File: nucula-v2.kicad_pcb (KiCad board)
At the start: 4 copper layers, 60 x 110 mm, 131 parts, among them J1 USB4105-GF-A-120, J2 JST-PH / 1S Li-ion, J3 KEYBOARD / USER FIT, J4 MAIN LINK / OPTIONAL, J5 MODULE LINK / OPTIONAL, Q1 IRLML6402, Q2 BSS138, Q3 IRLML6402, Q4 BSS138, Q5 BSS138, SW1 RESET, SW2 BOOT, U1 TP4054-42-SOT25R, U10 TS3USB30EDGSR, U2 SY8089AAAC, U3 ESP32-C3-WROOM-02-N4, U4 TPD2E2U06QDCKRQ1, U5 TLV803EA30DBZR, U6 PN7160A1HN/C100E, U7 AP3012KTR-E1, U8 PCF8574T, U9 MCP1700T-3002E/TT, Y1 27.12MHz / CL 10pF

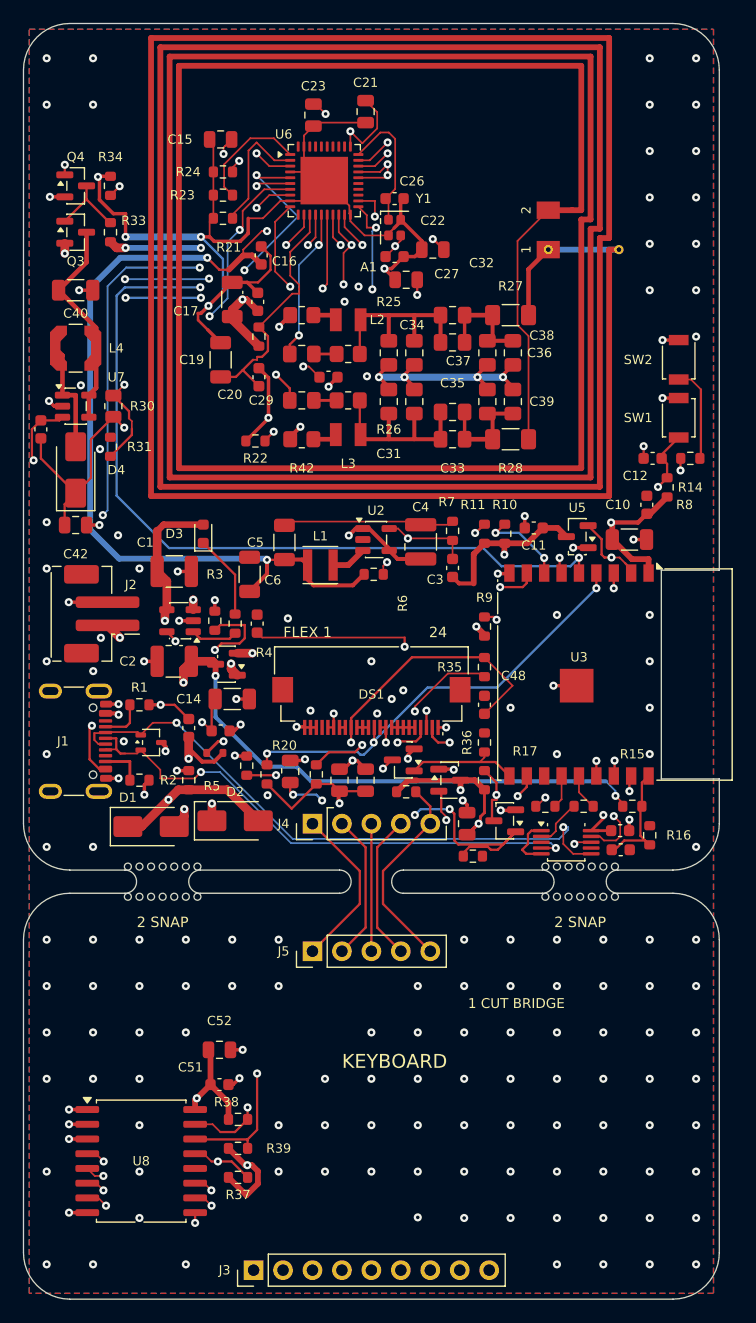
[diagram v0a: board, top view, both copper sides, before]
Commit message: Switch to ESP32-C3-MINI-1 with a flush antenna cutout
Replace WROOM-02 with MINI-1-H4X while preserving GPIO assignments and
4 MB flash. Resize the antenna notch and align the antenna tip with the
PCB edge; update the schematic, routing, footprint, model and BOM.

Include the current JST-SH battery connector and direct battery solder
pads, plus manufacturing archives and the new MINI prototype package.
Record ESP-IDF 5.4+ compatibility and the remaining physical validation.

Validation: zero ERC/DRC errors or unconnected nets; 17 MINI checks,
16 fabrication checks, six routing checks and 30 export checks pass.
The 261 scoped simulation cases completed without solver errors.
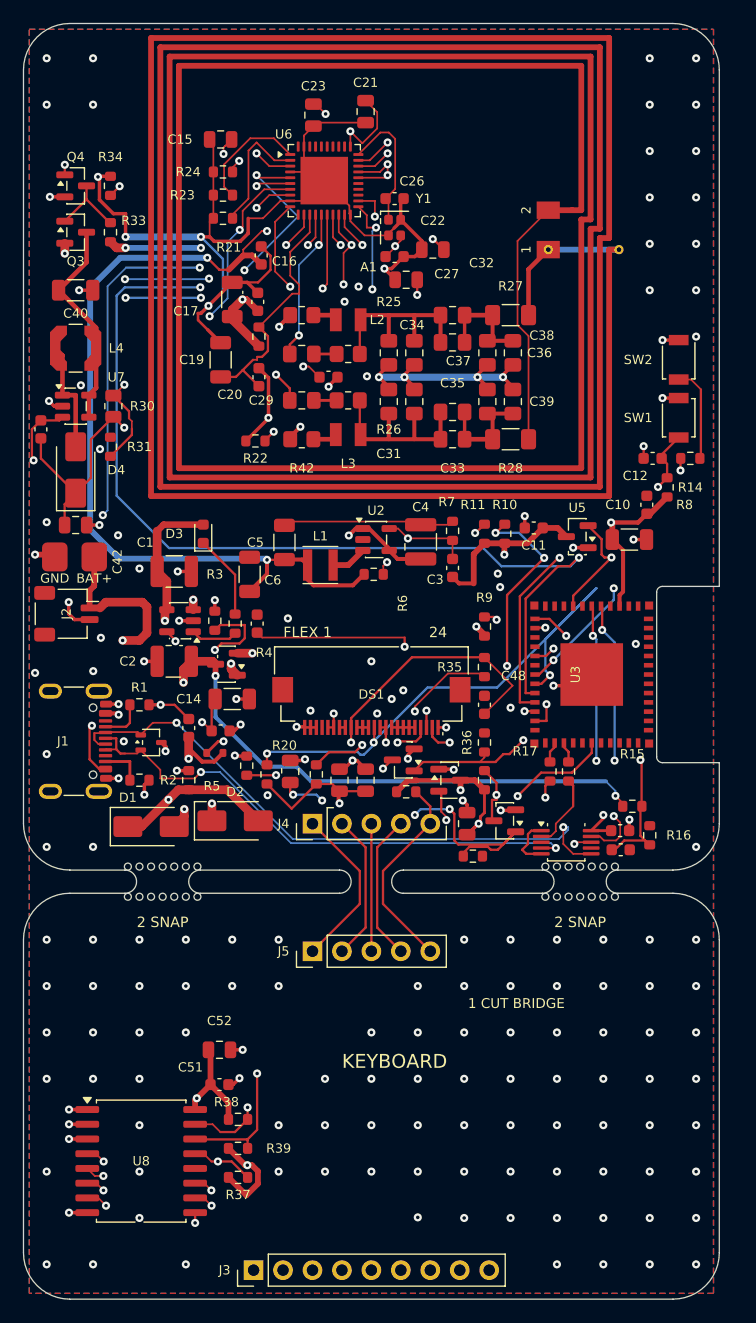
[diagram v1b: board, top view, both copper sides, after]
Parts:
- added J6: Battery wire pads, Nucula_Project:Battery_Lead_SolderPads_2x2.2x2.5mm_P3.4mm, F.Cu at (54.4, 96.0)
- J2: value JST-PH / 1S Li-ion -> JST-SH / 1S Li-ion; footprint Nucula_Project:JST_PH_B2B-PH-SM4-TB_1x02-1MP_P2.00mm_Vertical -> Nucula_Project:JST_SH_SM02B-SRSS-TB_1x02-1MP_P1.00mm_Horizontal
- U3: value ESP32-C3-WROOM-02-N4 -> ESP32-C3-MINI-1-H4X; footprint Nucula_Project:ESP32-C3-WROOM-02-N4_NoEPADSolder -> Nucula_Project:ESP32-C3-MINI-1-H4X_NoEPADSolder
- moved U3 3.80 mm to (101.7, 106.1)
- moved R13 3.27 mm to (97.0, 114.5), turned to 90 degrees
- moved J2 3.05 mm to (53.7, 100.9), turned to -90 degrees
- moved R12 3.03 mm to (95.4, 114.5), turned to 90 degrees
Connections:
- U3 pad 1: /+3V3 -> GND
- U3 pad 10: /OLED_RESET -> unconnected-(U3-NC-Pad10)
- U3 pad 11: /KEY_INT_N -> GND
- U3 pad 12: unconnected-(U3-IO21/TXD-Pad12) -> /Power + ESP32-C3/VBAT_ADC
- U3 pad 13: Net-(U3-IO18) -> /Power + ESP32-C3/USB_PRESENT_N
- U3 pad 14: Net-(U3-IO19) -> GND
- U3 pad 15: /OLED_PWR_EN -> unconnected-(U3-NC-Pad15)
- U3 pad 16: /Power + ESP32-C3/STRAP_GPIO2 -> /OLED_RESET
- U3 pad 17: /Power + ESP32-C3/USB_PRESENT_N -> unconnected-(U3-NC-Pad17)
- U3 pad 18: /Power + ESP32-C3/VBAT_ADC -> /I2C_SDA
- U3 pad 19: GND -> /I2C_SCL
- U3 pad 2: /Power + ESP32-C3/ESP_EN -> GND
- U3 pad 3: /I2C_SDA -> /+3V3
- U3 pad 4: /I2C_SCL -> unconnected-(U3-NC-Pad4)
- U3 pad 5: /NFC_IRQ -> /Power + ESP32-C3/STRAP_GPIO2
- U3 pad 6: /NFC_VEN -> /OLED_PWR_EN
- U3 pad 7: /Power + ESP32-C3/STRAP_GPIO8 -> unconnected-(U3-NC-Pad7)
- U3 pad 8: /Power + ESP32-C3/BOOT_N -> /Power + ESP32-C3/ESP_EN
- U3 pad 9: GND -> unconnected-(U3-NC-Pad9)
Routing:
- net /Power + ESP32-C3/VBAT_ADC: track 10.4 -> 28.2 mm, vias 0 -> 2
- net /Power + ESP32-C3/USB_PRESENT_N: track 26.2 -> 42.9 mm
- net /Power + ESP32-C3/STRAP_GPIO8: track 7.51 -> 22.3 mm, vias 2 -> 4
- net /NFC_VEN: track 105.6 -> 119.4 mm
- net /NFC_IRQ: track 83.8 -> 97.5 mm
- net /OLED_RESET: track 10.1 -> 23.0 mm, vias 0 -> 2
- net /Power + ESP32-C3/VBAT: track 64.5 -> 77.2 mm
- net /Power + ESP32-C3/STRAP_GPIO2: track 18.9 -> 31.3 mm, vias 2 -> 3
- net /OLED_PWR_EN: track 100.0 -> 112.2 mm, vias 4 -> 5
- net /Power + ESP32-C3/BOOT_N: track 31.2 -> 42.1 mm, vias 3 -> 4
- net /I2C_SCL: track 166.0 -> 175.8 mm
- net /I2C_SDA: track 164.0 -> 173.2 mm, vias 8 -> 9
- net /KEY_INT_N: track 59.7 -> 66.5 mm
- net /Power + ESP32-C3/ESP_EN: track 19.5 -> 22.6 mm
- net /Power + ESP32-C3/USB_PHY_D+: track 4.26 -> 6.55 mm
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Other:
- outline, holes or cut-outs redrawn

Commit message: Add six M2 mounting holes and validate the hardware revision
Place 2.2 mm NPTH holes at all four main-board corners and the two
lower keyboard corners. Reserve 5.5 mm copper and component clearances
for hardware up to 5 mm across, and move R16 with local ADC rerouting.
Preserve the MINI antenna fit, board outline and breakaway connections.

Add mechanical clearance checks, a dimensioned mounting plan and the
mounting-2026-10-08 manufacturing package with verified drill data.

Validation: zero ERC/DRC errors, unconnected nets or parity findings;
10 mounting checks, 32 export checks and 13 regression tests pass.
All 261 scoped simulations complete without solver errors. Existing
cosmetic warnings and USB layout advisories are unchanged.
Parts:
- added H1: M2 2.2mm NPTH, Nucula_Project:MountingHole_2.2mm_M2_5.5mm_Keepout, F.Cu at (53.5, 53.5)
- added H2: M2 2.2mm NPTH, Nucula_Project:MountingHole_2.2mm_M2_5.5mm_Keepout, F.Cu at (106.5, 53.5)
- added H3: M2 2.2mm NPTH, Nucula_Project:MountingHole_2.2mm_M2_5.5mm_Keepout, F.Cu at (53.5, 120.0)
- added H4: M2 2.2mm NPTH, Nucula_Project:MountingHole_2.2mm_M2_5.5mm_Keepout, F.Cu at (106.5, 120.0)
- added H5: M2 2.2mm NPTH, Nucula_Project:MountingHole_2.2mm_M2_5.5mm_Keepout, F.Cu at (53.5, 156.5)
- added H6: M2 2.2mm NPTH, Nucula_Project:MountingHole_2.2mm_M2_5.5mm_Keepout, F.Cu at (106.5, 156.5)
- moved R16 4.37 mm to (105.0, 115.8)
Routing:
- net GND: vias 174 -> 163

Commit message: Label PCB buttons BOOT and RESET on the silkscreen
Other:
- board text added: "BOOT"
- board text added: "RESET"
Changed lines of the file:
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@@
 		(tags "Tactile Switch")
 		(property "Reference" "SW1"
-			(at 0 -3.5 0)
-			(layer "F.SilkS")
+			(at 0 0 0)
+			(layer "F.Fab")
 			(effects
 				(font
@@
 			(layer "F.Fab")
 		)
-		(fp_text user "${REFERENCE}"
-			(at 0 -2.5 90)
-			(layer "F.Fab")
-			(effects
-				(font
-					(size 1 1)
-					(thickness 0.15)
-				)
-			)
-		)
 		(pad "1" smd rect
 			(at -1.7 0 90)
@@
 		(tags "Tactile Switch")
 		(property "Reference" "SW2"
-			(at 0 -3.5 0)
-			(layer "F.SilkS")
+			(at 0 0 0)
+			(layer "F.Fab")
 			(effects
 				(font
@@
 			(layer "F.Fab")
 		)
-		(fp_text user "${REFERENCE}"
-			(at 0 -2.5 90)
-			(layer "F.Fab")
-			(effects
-				(font
-					(size 1 1)
-					(thickness 0.15)
-				)
-			)
-		)
 		(pad "1" smd rect
 			(at -1.7 0 90)
@@
 		(layer "Edge.Cuts")
 	)
+	(gr_text "RESET"
+		(at 103 84 0)
+		(layer "F.SilkS")
+		(effects
+			(font
+				(size 0.8 0.8)
+				(thickness 0.12)
+			)
+		)
+	)
+	(gr_text "BOOT"
+		(at 103 79 0)
+		(layer "F.SilkS")
+		(effects
+			(font
+				(size 0.8 0.8)
+				(thickness 0.12)
+			)
+		)
+	)
 	(gr_text "1 CUT BRIDGE"

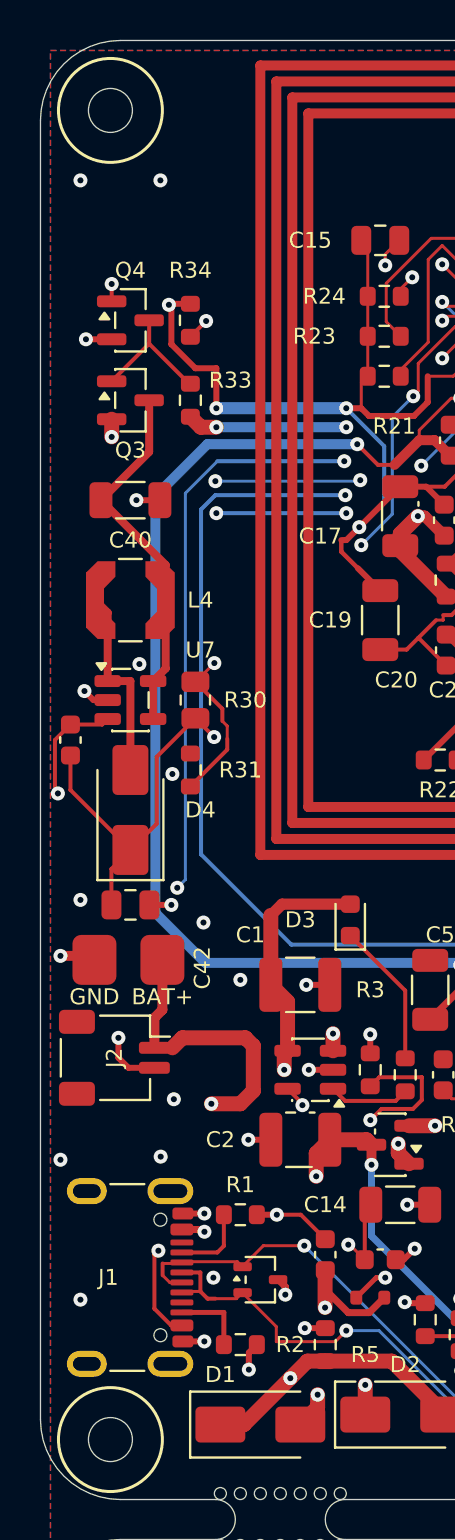
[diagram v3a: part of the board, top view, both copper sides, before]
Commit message: move jst connector, add notch for batt cable
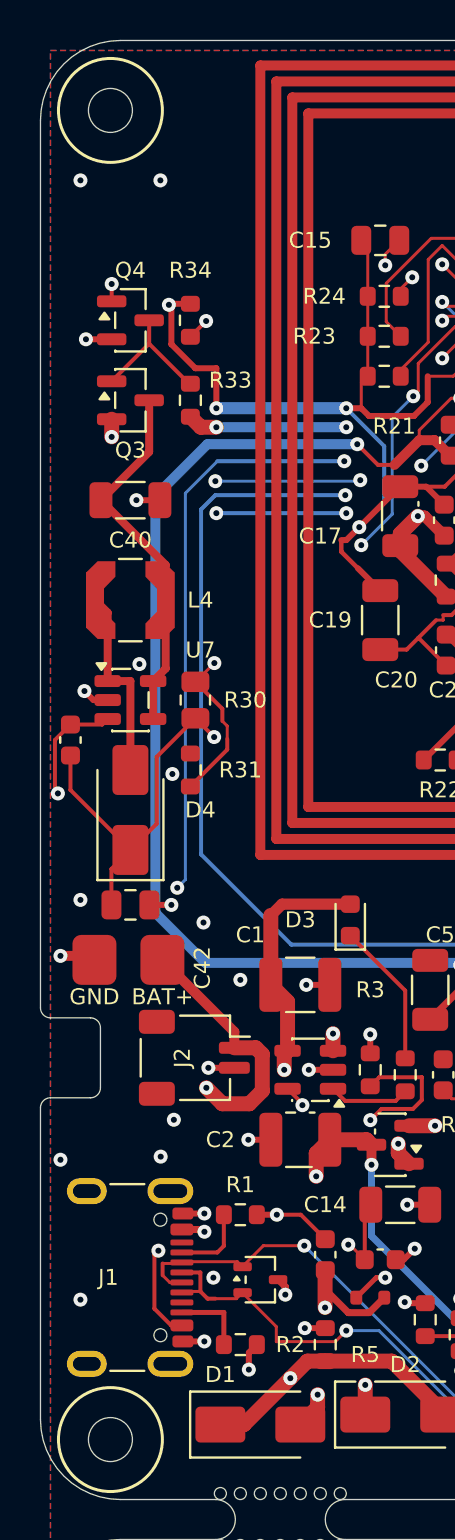
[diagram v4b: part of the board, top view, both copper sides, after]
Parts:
- moved J2 4.00 mm to (57.7, 100.9)
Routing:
- net GND: track 250.2 -> 248.5 mm
- net /Power + ESP32-C3/VBAT: track 77.2 -> 75.9 mm
- net /I2C_SCL: track 175.8 -> 176.4 mm
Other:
- outline, holes or cut-outs redrawn
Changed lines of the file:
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@@
 		(locked yes)
 		(layer "F.Cu")
-		(at 53.7 100.9 -90)
+		(at 57.7 100.9 -90)
 		(descr "JST SH series connector, SM02B-SRSS-TB (http://www.jst-mfg.com/product/pdf/eng/eSH.pdf)")
 		(tags "connector JST SH horizontal")
 		(property "Reference" "J2"
-			(at 0 0 90)
+			(at 0 0.6 90)
 			(layer "F.SilkS")
 			(effects
@@
 		(layer "Dwgs.User")
 	)
+	(gr_line
+		(start 50 54)
+		(end 50 98.4)
+		(stroke
+			(width 0.05)
+			(type default)
+		)
+		(layer "Edge.Cuts")
+	)
 	(gr_arc
 		(start 50 54)
@@
 	)
 	(gr_line
-		(start 50 119)
-		(end 50 54)
+		(start 50 103.4)
+		(end 50 119)
 		(stroke
 			(width 0.05)
-			(type solid)
+			(type default)
+		)
+		(layer "Edge.Cuts")
+	)
+	(gr_arc
+		(start 50 103.4)
+		(mid 50.146447 103.046447)
+		(end 50.5 102.9)
+		(stroke
+			(width 0.05)
+			(type default)
 		)
 		(layer "Edge.Cuts")
@@
 		(layer "Edge.Cuts")
 	)
+	(gr_arc
+		(start 50.5 98.9)
+		(mid 50.146447 98.753553)
+		(end 50 98.4)
+		(stroke
+			(width 0.05)
+			(type default)
+		)
+		(layer "Edge.Cuts")
+	)
+	(gr_line
+		(start 50.5 98.9)
+		(end 52.5 98.9)
+		(stroke
+			(width 0.05)
+			(type default)
+		)
+		(layer "Edge.Cuts")
+	)
+	(gr_arc
+		(start 52.5 98.9)
+		(mid 52.853553 99.046447)
+		(end 53 99.4)
+		(stroke
+			(width 0.05)
+			(type default)
+		)
+		(layer "Edge.Cuts")
+	)
+	(gr_line
+		(start 52.5 102.9)
+		(end 50.5 102.9)
+		(stroke
+			(width 0.05)
+			(type default)
+		)
+		(layer "Edge.Cuts")
+	)
+	(gr_line
+		(start 53 99.4)
+		(end 53 102.4)
+		(stroke
+			(width 0.05)
+			(type default)
+		)
+		(layer "Edge.Cuts")
+	)
+	(gr_arc
+		(start 53 102.4)
+		(mid 52.853553 102.753553)
+		(end 52.5 102.9)
+		(stroke
+			(width 0.05)
+			(type default)
+		)
+		(layer "Edge.Cuts")
+	)
 	(gr_line
 		(start 54 50)
@@
 		(layer "Edge.Cuts")
 	)
-	(gr_text "RESET"
-		(at 103 84 0)
+	(gr_text "BOOT"
+		(at 103 79 0)
 		(layer "F.SilkS")
 		(effects
@@
 		)
 	)
-	(gr_text "BOOT"
-		(at 103 79 0)
+	(gr_text "RESET"
+		(at 103 84 0)
 		(layer "F.SilkS")
 		(effects
@@
 	)
 	(segment
-		(start 54.4 101.4)
-		(end 55.7 101.4)
-		(width 0.3)
-		(layer "F.Cu")
-		(net "GND")
-	)
-	(segment
 		(start 78.1 66.4)
 		(end 78.1875 66.4875)
@@
 	)
 	(segment
+		(start 59.7 101.4)
+		(end 58.4 101.4)
+		(width 0.3)
+		(layer "F.Cu")
+		(net "GND")
+	)
+	(segment
 		(start 65.95 74.35)
 		(end 67.975 72.325)
@@
 	)
 	(segment
-		(start 53.9 100.9)
-		(end 54.4 101.4)
-		(width 0.3)
-		(layer "F.Cu")
-		(net "GND")
-	)
-	(segment
 		(start 60.425 115.65)
 		(end 60.825 115.25)
@@
 	)
 	(segment
-		(start 53.9 99.9)
-		(end 53.9 100.9)
-		(width 0.3)
-		(layer "F.Cu")
-		(net "GND")
-	)
-	(segment
 		(start 87.05 114.3)
 		(end 87.1 114.35)
@@
 	)
 	(via
-		(at 53.9 99.9)
+		(at 58.4 101.4)
 		(size 0.7)
 		(drill 0.3)
@@
 	)
 	(via
-		(at 56.6734 102.972)
+		(at 56.6734 104)
 		(size 0.7)
 		(drill 0.3)
@@
 	)
 	(segment
+		(start 60.7194 108.046)
+		(end 61.7474 108.046)
+		(width 0.2)
+		(layer "In1.Cu")
+		(net "/I2C_SCL")
+	)
+	(segment
 		(start 62.1779 108.046)
 		(end 69.04195 114.91005)
@@
 	)
 	(segment
-		(start 56.6734 102.972)
-		(end 61.7474 108.046)
+		(start 56.6734 104)
+		(end 60.7194 108.046)
 		(width 0.2)
 		(layer "In1.Cu")
@@
 	)
 	(segment
-		(start 57.5 102.1454)
+		(start 57.5 103.1734)
 		(end 57.5 73.3)
 		(width 0.15)
@@
 	)
 	(segment
-		(start 80.2 111.999)
-		(end 82.54 114.339)
-		(width 0.2)
+		(start 56.6734 104)
+		(end 57.5 103.1734)
+		(width 0.15)
 		(layer "In2.Cu")
 		(net "/I2C_SCL")
 	)
 	(segment
-		(start 56.6734 102.972)
-		(end 57.5 102.1454)
-		(width 0.15)
+		(start 80.2 111.999)
+		(end 82.54 114.339)
+		(width 0.2)
 		(layer "In2.Cu")
 		(net "/I2C_SCL")
@@
 	)
 	(segment
-		(start 60.65 100.3)
-		(end 60.65 102.55)
-		(width 0.75)
+		(start 56.1 96)
+		(end 59.7 99.6)
+		(width 0.5)
 		(layer "F.Cu")
 		(net "/Power + ESP32-C3/VBAT")
 	)
 	(segment
-		(start 60.25 99.9)
-		(end 60.65 100.3)
+		(start 61.1 100.725)
+		(end 61.1 102.55)
 		(width 0.75)
 		(layer "F.Cu")
@@
 	)
 	(segment
-		(start 55.7 98.9)
-		(end 55.7 100.4)
-		(width 0.5)
-		(layer "F.Cu")
-		(net "/Power + ESP32-C3/VBAT")
-	)
-	(segment
-		(start 101.675 117.225)
-		(end 101.675 117.5)
-		(width 0.15)
+		(start 60.45 103.2)
+		(end 59.1 103.2)
+		(width 0.75)
 		(layer "F.Cu")
 		(net "/Power + ESP32-C3/VBAT")
 	)
 	(segment
-		(start 60 103.2)
-		(end 58.55 103.2)
+		(start 61.1 102.55)
+		(end 60.45 103.2)
 		(width 0.75)
 		(layer "F.Cu")
@@
 	)
 	(segment
-		(start 55.7 100.4)
-		(end 56.6 100.4)
-		(width 0.4)
+		(start 101.675 117.225)
+		(end 101.675 117.5)
+		(width 0.15)
 		(layer "F.Cu")
 		(net "/Power + ESP32-C3/VBAT")
@@
 	)
 	(segment
-		(start 57.1 99.9)
-		(end 60.25 99.9)
+		(start 59.7 99.6)
+		(end 59.7 100.4)
+		(width 0.5)
+		(layer "F.Cu")
+		(net "/Power + ESP32-C3/VBAT")
+	)
+	(segment
+		(start 60.775 100.4)
+		(end 61.1 100.725)
 		(width 0.75)
 		(layer "F.Cu")
@@
 	)
 	(segment
-		(start 60.65 102.55)
-		(end 60 103.2)
+		(start 59.7 100.4)
+		(end 60.775 100.4)
 		(width 0.75)
 		(layer "F.Cu")
@@
 	)
 	(segment
-		(start 56.6 100.4)
-		(end 57.1 99.9)
-		(width 0.75)
-		(layer "F.Cu")
-		(net "/Power + ESP32-C3/VBAT")
-	)
-	(segment
-		(start 56.1 96)
-		(end 56.1 98.5)
-		(width 0.5)
-		(layer "F.Cu")
-		(net "/Power + ESP32-C3/VBAT")
-	)
-	(segment
 		(start 63.7957 106.83)
 		(end 63.7957 105.6793)
@@
 	)
 	(segment
-		(start 56.1 98.5)
-		(end 55.7 98.9)
-		(width 0.5)
+		(start 59.1 103.2)
+		(end 58.3 102.4)
+		(width 0.75)
 		(layer "F.Cu")
 		(net "/Power + ESP32-C3/VBAT")
@@
 	)
 	(via
-		(at 58.55 103.2)
+		(at 58.3 102.4)
 		(size 0.7)
 		(drill 0.3)
@@
 	)
 	(segment
-		(start 58.55 103.2)
+		(start 59.1 103.2)
 		(end 60.1657 103.2)
 		(width 0.75)
 		(layer "In1.Cu")
+		(net "/Power + ESP32-C3/VBAT")
+	)
+	(segment
+		(start 59.1 103.2)
+		(end 58.3 102.4)
+		(width 0.75)
+		(layer "In1.Cu")
